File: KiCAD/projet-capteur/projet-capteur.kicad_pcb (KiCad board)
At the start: 2 copper layers, 68.6 x 53.3 mm, 22 parts, among them J1 Power, J2 Analog, J3 Digital/PWM, J4 Digital/PWM, U2 LTC1050

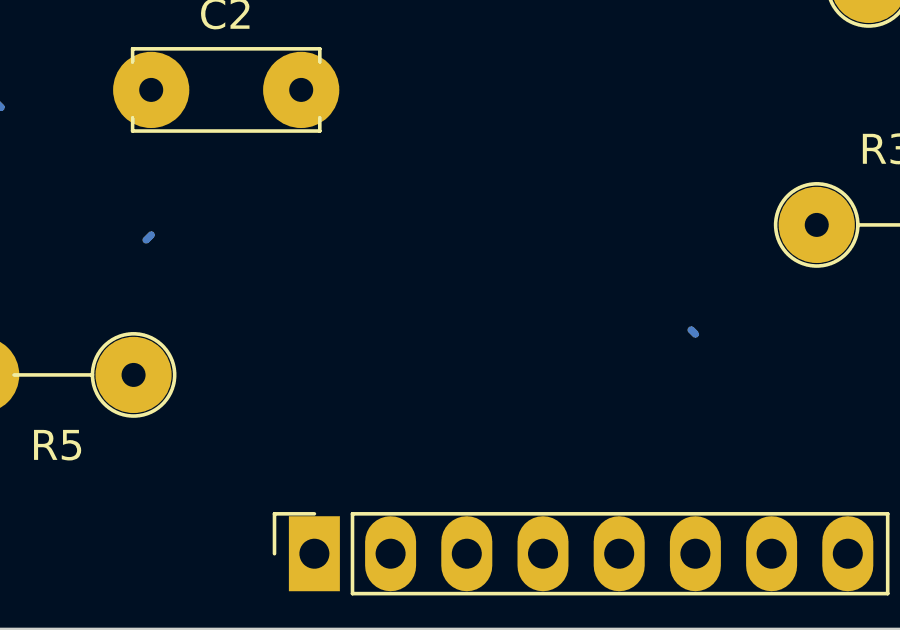
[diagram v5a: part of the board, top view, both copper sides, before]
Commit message: Ajout du header Servo Moteur
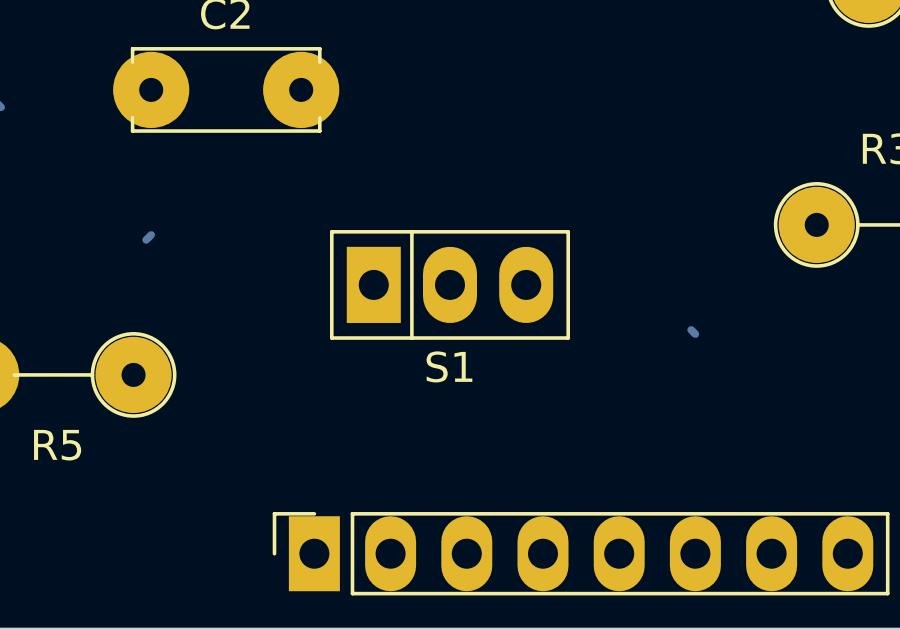
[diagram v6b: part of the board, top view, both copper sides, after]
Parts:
- added S1: ~, MyLibEmpreinte:ServoMoteur, F.Cu at (132.5, 88.5)
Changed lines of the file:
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@@
+		)
+	)
+	(footprint "MyLibEmpreinte:ServoMoteur"
+		(layer "F.Cu")
+		(at 132.46 88.5)
+		(property "Reference" "S1"
+			(at 0 2.77 0)
+			(layer "F.SilkS")
+			(effects
+				(font
+					(size 1 1)
+					(thickness 0.15)
+				)
+			)
+		)
+		(property "Value" "~"
+			(at 0 -2.77 0)
+			(layer "F.Fab")
+			(effects
+				(font
+					(size 1 1)
+					(thickness 0.15)
+				)
+			)
+		)
+		(property "Datasheet" ""
+			(at 0 0 0)
+			(layer "F.Fab")
+			(hide yes)
+			(effects
+				(font
+					(size 1.27 1.27)
+					(thickness 0.15)
+				)
+			)
+		)
+		(property "Description" ""
+			(at 0 0 0)
+			(layer "F.Fab")
+			(hide yes)
+			(effects
+				(font
+					(size 1.27 1.27)
+					(thickness 0.15)
+				)
+			)
+		)
+		(sheetname "/")
+		(sheetfile "projet-capteur.kicad_sch")
+		(attr through_hole)
+		(fp_line
+			(start -3.94 -1.77)
+			(end 3.94 -1.77)
+			(stroke
+				(width 0.12)
+				(type default)
+			)
+			(layer "F.SilkS")
+		)
+		(fp_line
+			(start -3.94 1.77)
+			(end -3.94 -1.77)
+			(stroke
+				(width 0.12)
+				(type default)
+			)
+			(layer "F.SilkS")
+		)
+		(fp_line
+			(start -1.27 -1.77)
+			(end -1.27 1.77)
+			(stroke
+				(width 0.12)
+				(type default)
+			)
+			(layer "F.SilkS")
+		)
+		(fp_line
+			(start 3.94 -1.77)
+			(end 3.94 1.77)
+			(stroke
+				(width 0.12)
+				(type default)
+			)
+			(layer "F.SilkS")
+		)
+		(fp_line
+			(start 3.94 1.77)
+			(end -3.94 1.77)
+			(stroke
+				(width 0.12)
+				(type default)
+			)
+			(layer "F.SilkS")
+		)
+		(fp_line
+			(start -3.69 -1.52)
+			(end 3.69 -1.52)
+			(stroke
+				(width 0.05)
+				(type default)
+			)
+			(layer "F.CrtYd")
+		)
+		(fp_line
+			(start -3.69 1.52)
+			(end -3.69 -1.52)
+			(stroke
+				(width 0.05)
+				(type default)
+			)
+			(layer "F.CrtYd")
+		)
+		(fp_line
+			(start 3.69 -1.52)
+			(end 3.69 1.52)
+			(stroke
+				(width 0.05)
+				(type default)
+			)
+			(layer "F.CrtYd")
+		)
+		(fp_line
+			(start 3.69 1.52)
+			(end -3.69 1.52)
+			(stroke
+				(width 0.05)
+				(type default)
+			)
+			(layer "F.CrtYd")
+		)
+		(pad "1" thru_hole rect
+			(at -2.54 0)
+			(size 1.8 2.54)
+			(drill 1)
+			(layers "*.Cu" "*.Mask")
+			(remove_unused_layers no)
+			(net 16 "/*11")
+			(pinfunction "Data")
+			(pintype "input")
+			(thermal_bridge_angle 45)
+		)
+		(pad "2" thru_hole oval
+			(at 0 0)
+			(size 1.8 2.54)
+			(drill 1)
+			(layers "*.Cu" "*.Mask")
+			(remove_unused_layers no)
+			(net 3 "5V")
+			(pinfunction "Vcc")
+			(pintype "input")
+			(thermal_bridge_angle 45)
+		)
+		(pad "3" thru_hole oval
+			(at 2.54 0)
+			(size 1.8 2.54)
+			(drill 1)
+			(layers "*.Cu" "*.Mask")
+			(remove_unused_layers no)
+			(net 1 "GND")
+			(pinfunction "GND")
+			(pintype "input")
+			(thermal_bridge_angle 45)
+		)
+		(embedded_fonts no)
+		(model "${KICAD9_3DMODEL_DIR}/Connector_PinHeader_2.54mm.3dshapes/PinHeader_1x03_P2.54mm_Vertical.wrl"
+			(offset
+				(xyz -2.5 0 0)
+			)
+			(scale
+				(xyz 1 1 1)
+			)
+			(rotate
+				(xyz -0 -0 -90)
+			)
 		)
 	)

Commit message: Seance Realisation du shield 12.03
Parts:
- added REF**: Rotary Encoder, MyLibEmpreinte:Rotary Encoder, F.Cu at (103.5, 75.5)
- moved U3 45.8 mm to (122.0, 55.5), turned to 0 degrees
- moved FS1 42.9 mm to (110.0, 83.0), turned to 90 degrees
- moved R6 34.3 mm to (114.5, 91.0)
- moved R1 24.3 mm to (134.0, 87.0)
- moved R2 12.0 mm to (112.0, 70.9), turned to -90 degrees
- moved C3 9.28 mm to (118.5, 85.5), turned to 90 degrees
- moved R5 8.20 mm to (127.5, 85.5)
- moved R4 8.16 mm to (134.5, 62.0), turned to 0 degrees
- moved R3 8.10 mm to (138.0, 81.9), turned to -90 degrees
- moved S1 6.08 mm to (138.0, 91.0)
- moved U1 4.54 mm to (162.5, 74.3), turned to -90 degrees
- moved C1 3.73 mm to (115.5, 71.0)
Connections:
- net Output Capteur renamed ADC
- MCP1 pad 1: unconnected-(MCP1-CS-Pad1) -> /*10
- MCP1 pad 2: unconnected-(MCP1-SCK-Pad2) -> /13
- MCP1 pad 3: unconnected-(MCP1-SDI-Pad3) -> /*11
- R1 pad 1: unconnected-(R1-Pad1) -> Sortie Capteur
- S1 pad 1: /*11 -> /*9
- U3 pad 4: unconnected-(U3-Tx-Pad4) -> /*3
- U3 pad 5: unconnected-(U3-Rx-Pad5) -> /2
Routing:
- net Net-(C2-Pad2): track 0.24 -> 16.3 mm
- net GND: track 1.89 -> 0.00 mm
- net Net-(U2-+): track 1.00 -> 0.00 mm
- net Net-(U2--): track 0.74 -> 0.00 mm

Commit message: Seance Realisation du shield 12.03 v2
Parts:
- removed R3: 1k, Resistor_THT:R_Axial_DIN0207_L6.3mm_D2.5mm_P5.08mm_Vertical
- removed REF**: Rotary Encoder, MyLibEmpreinte:Rotary Encoder
- added C4: C, Capacitor_THT:C_Disc_D6.0mm_W2.5mm_P5.00mm, F.Cu at (163.0, 59.5)
- added CG1: ~, MyLibEmpreinte:Capteur Graphene, F.Cu at (128.2, 91.5)
- added ROE1: ~, MyLibEmpreinte:RotaryEncoder, F.Cu at (154.0, 54.5)
- R6: value R -> 10k
- moved S1 36.3 mm to (128.5, 56.0), turned to 180 degrees
- moved U3 16.6 mm to (106.5, 61.5), turned to 90 degrees
- moved FS1 14.2 mm to (120.5, 92.6)
- moved R6 8.51 mm to (108.0, 85.5), turned to 90 degrees
- moved C2 7.07 mm to (127.5, 77.0), turned to -90 degrees
- moved C3 6.00 mm to (112.5, 85.5)
- moved MCP1 5.10 mm to (121.4, 63.7)
- moved U1 4.90 mm to (164.4, 78.8)
- moved R4 3.33 mm to (135.9, 65.0)
- moved U2 1.94 mm to (134.8, 68.9)
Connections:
- C2 pad 1: Net-(U2-+) -> R3
- FS1 pad 1: Net-(FS1-FlexPin) -> Sortie Flex
- J2 pad 2: /A1 -> Sortie Flex
- J3 pad 10: /8 -> TX
- J4 pad 1: /7 -> RX
- J4 pad 2: /*6 -> ROE 3
- J4 pad 4: /4 -> ROE 4
- J4 pad 6: /2 -> ROE 5
- MCP1 pad 5: unconnected-(MCP1-P0A-Pad5) -> R3
- MCP1 pad 6: unconnected-(MCP1-P0W-Pad6) -> GND
- MCP1 pad 7: unconnected-(MCP1-P0B-Pad7) -> GND
- R4 pad 1: Net-(U2-+) -> R3
- R6 pad 1: Net-(FS1-FlexPin) -> Sortie Flex
- U2 pad 3: Net-(U2-+) -> R3
- U3 pad 4: /*3 -> TX
- U3 pad 5: /2 -> RX
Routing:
- net 5V: track 0.00 -> 208.7 mm, vias 0 -> 3
- net GND: track 0.00 -> 128.1 mm, vias 0 -> 6
- net ADC: track 0.00 -> 59.5 mm
- net Sortie Flex: track 0.00 -> 57.0 mm
- net TX: track 0.00 -> 53.4 mm
- net RX: track 0.00 -> 50.0 mm
- net Net-(U2--): track 0.00 -> 44.4 mm
- net /*11: track 0.00 -> 37.4 mm, vias 0 -> 2
- net R3: track 0.00 -> 30.7 mm
- net /*10: track 0.00 -> 26.0 mm, vias 0 -> 2
- net /13: track 0.00 -> 23.6 mm, vias 0 -> 2
- net SCL: track 0.00 -> 23.4 mm
- net Net-(C2-Pad2): track 16.3 -> 36.8 mm
- net SDA: track 0.00 -> 18.2 mm
- net /*9: track 0.00 -> 12.6 mm
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- added copper zone on B.Cu, net GND
